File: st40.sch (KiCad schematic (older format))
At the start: 13 parts, among them J1 USB_B_Mini, SW1 SW_SPST, SW2 SW_SPST, U1 LD1117S33TR_SOT223, U2 STM32F072CBTx

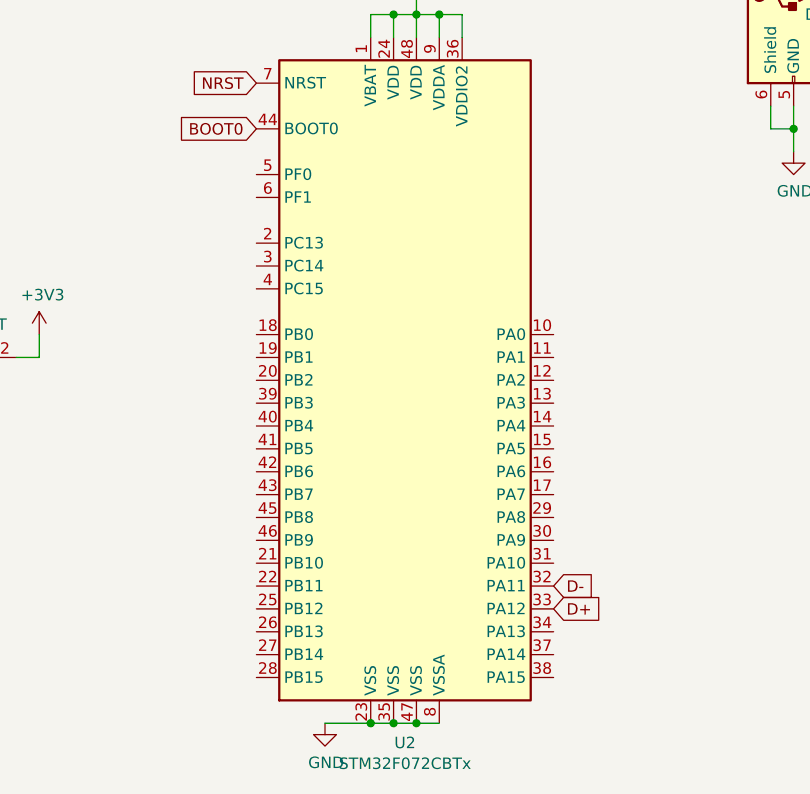
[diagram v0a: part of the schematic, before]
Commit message: fixed missing traces from col/rows to mcu, did some rerouting, fixed board outline
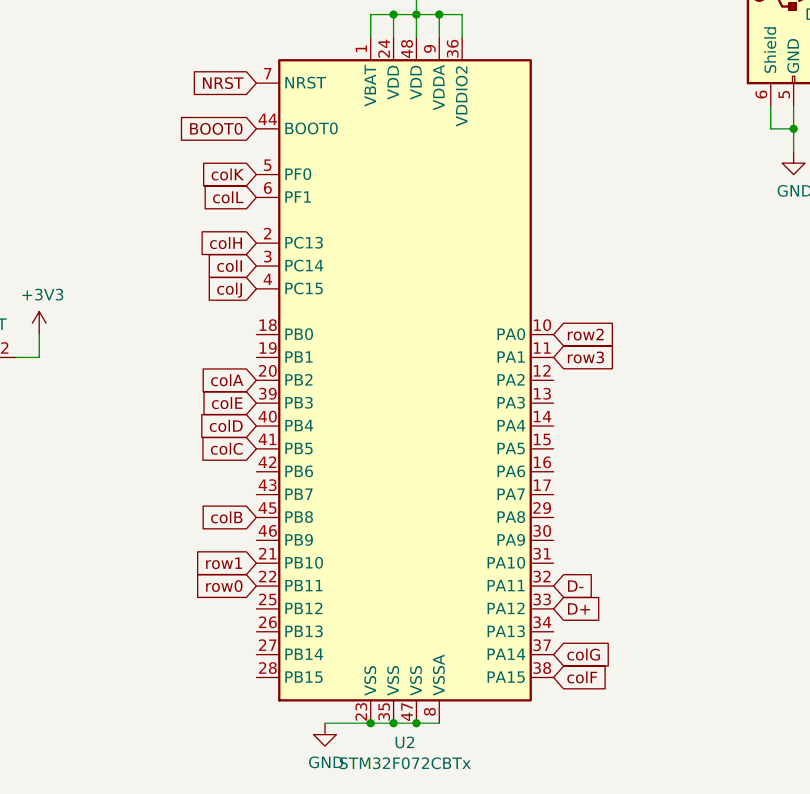
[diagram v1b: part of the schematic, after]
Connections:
- net row2: now reaches U2.10 (PA0)
- net row3: now reaches U2.11 (PA1)
- net colH: now reaches U2.2 (PC13)
- net colA: now reaches U2.20 (PB2)
- net row1: now reaches U2.21 (PB10)
- net row0: now reaches U2.22 (PB11)
- net colI: now reaches U2.3 (PC14)
- net colG: now reaches U2.37 (PA14)
- net colF: now reaches U2.38 (PA15)
- net colE: now reaches U2.39 (PB3)
- net colJ: now reaches U2.4 (PC15)
- net colD: now reaches U2.40 (PB4)
- net colC: now reaches U2.41 (PB5)
- net colB: now reaches U2.45 (PB8)
- net colK: now reaches U2.5 (PF0)
- net colL: now reaches U2.6 (PF1)
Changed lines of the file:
@@
 EESchema Schematic File Version 4
+LIBS:st40-cache
 EELAYER 26 0
 EELAYER END
@@
 Text GLabel 5600 4400 2    50   Input ~ 0
 D-
+Text GLabel 4300 4400 0    50   Input ~ 0
+row0
+Text GLabel 4300 4300 0    50   Input ~ 0
+row1
+Text GLabel 4300 4100 0    50   Input ~ 0
+colB
+Text GLabel 4300 3800 0    50   Input ~ 0
+colC
+Text GLabel 5600 3300 2    50   Input ~ 0
+row2
+Text GLabel 5600 3400 2    50   Input ~ 0
+row3
+Text GLabel 4300 2700 0    50   Input ~ 0
+colL
+Text GLabel 4300 2600 0    50   Input ~ 0
+colK
+Text GLabel 4300 3100 0    50   Input ~ 0
+colJ
+Text GLabel 4300 3000 0    50   Input ~ 0
+colI
+Text GLabel 4300 2900 0    50   Input ~ 0
+colH
+Text GLabel 4300 3700 0    50   Input ~ 0
+colD
+Text GLabel 4300 3600 0    50   Input ~ 0
+colE
+Text GLabel 5600 4800 2    50   Input ~ 0
+colF
+Text GLabel 5600 4700 2    50   Input ~ 0
+colG
+Text GLabel 4300 3500 0    50   Input ~ 0
+colA
 $EndSCHEMATC
